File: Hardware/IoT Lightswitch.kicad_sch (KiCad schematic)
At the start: 23 parts, among them J1 Screw_Terminal_01x04, J2 Conn_01x04, K1 SANYOU_SRD_Form_C, Q1 NMOS, SW1 SW_SPDT, SW2 SW_SPDT, SW3 SW_Push, SW4 SW_Push, SW5 SW_SPST, U1 ESP32-S2-SOLO-2

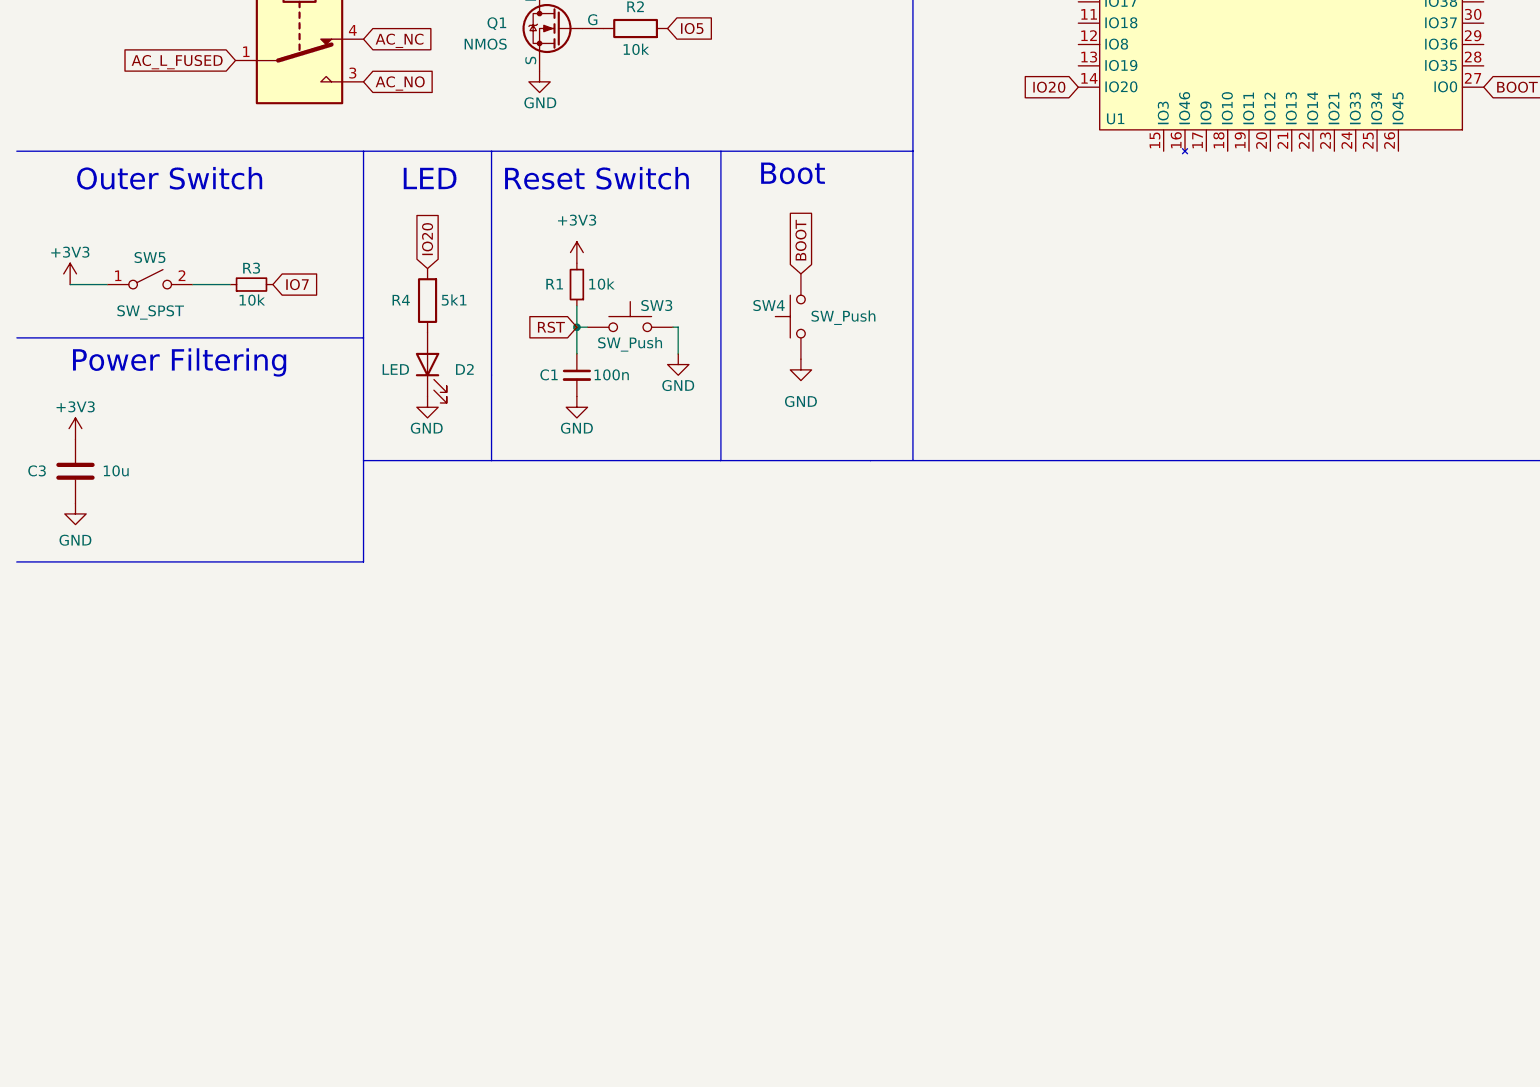
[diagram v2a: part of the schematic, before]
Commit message: Added Humidity and Temperature Sensor
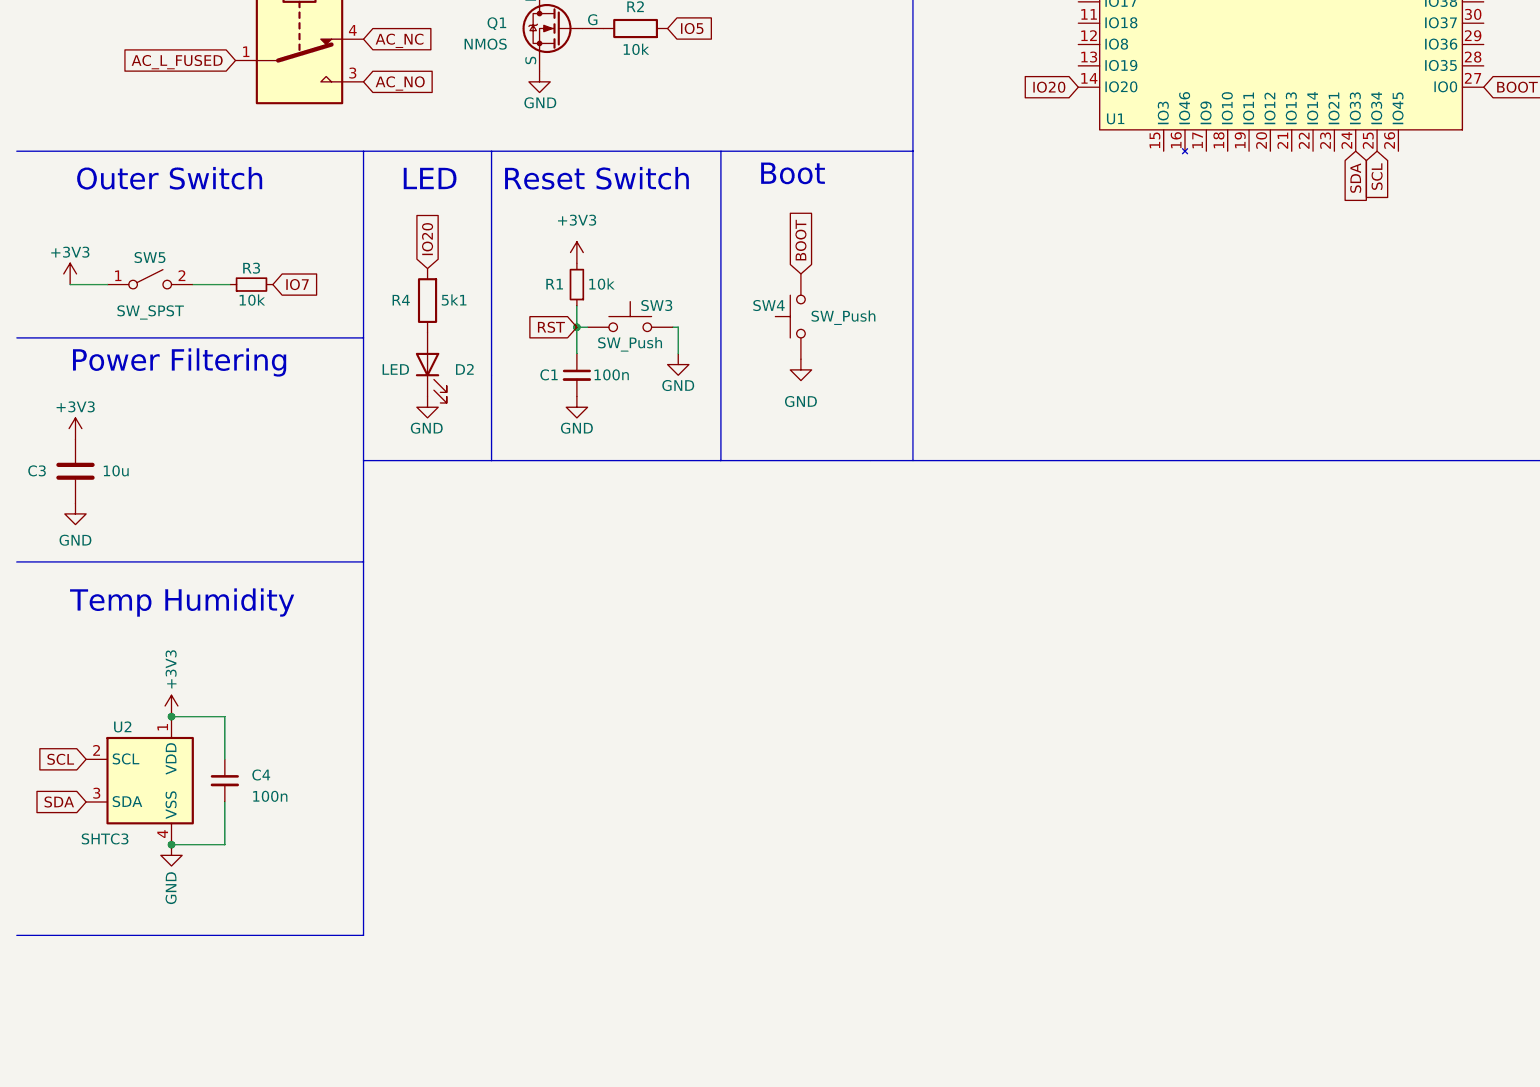
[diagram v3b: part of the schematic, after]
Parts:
- added C4: 100n, Capacitor_SMD:C_0402_1005Metric, symbol Device:C_Small
- added U2: SHTC3, Sensor_Humidity:Sensirion_DFN-4-1EP_2x2mm_P1mm_EP0.7x1.6mm, symbol Sensor_Humidity:SHTC3
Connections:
- net +3V3: now also C4.1, U2.1 (VDD)
- net GND: now also C4.2, U2.4 (VSS)
- net SDA: now reaches U1.24 (IO33)
- net SDA: now also U2.3 (SDA)
- net SCL: now reaches U1.25 (IO34)
- net SCL: now also U2.2 (SCL)
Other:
- note added: "Temp Humidity"
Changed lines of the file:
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@@
   (junction (at 86.995 30.48) (diameter 0) (color 0 0 0 0)
   )
+  (junction (at 31.115 161.29) (diameter 0) (color 0 0 0 0)
+  )
   (junction (at 187.96 36.83) (diameter 0) (color 0 0 0 0)
   )
@@
   )
   (junction (at 53.975 49.53) (diameter 0) (color 0 0 0 0)
+  )
+  (junction (at 31.115 146.05) (diameter 0) (color 0 0 0 0)
   )
   (junction (at 86.995 25.4) (diameter 0) (color 0 0 0 0)
@@
     (stroke (width 0) (type default))
   )
+  (polyline (pts (xy 12.7 172.085) (xy 53.975 172.085))
+    (stroke (width 0) (type default))
+  )
   (wire (pts (xy 91.44 102.87) (xy 91.44 99.695))
     (stroke (width 0) (type default))
   )
+  (wire (pts (xy 37.465 156.21) (xy 37.465 161.29))
+    (stroke (width 0) (type default))
+  )
   (wire (pts (xy 79.375 97.155) (xy 79.375 99.695))
     (stroke (width 0) (type default))
@@
     (stroke (width 0) (type default))
   )
+  (wire (pts (xy 37.465 161.29) (xy 31.115 161.29))
+    (stroke (width 0) (type default))
+  )
   (polyline (pts (xy 375.285 12.7) (xy 375.285 40.64))
     (stroke (width 0) (type default))
@@
   )
   (polyline (pts (xy 62.23 37.465) (xy 119.38 37.465))
+    (stroke (width 0) (type default))
+  )
+  (wire (pts (xy 31.115 146.05) (xy 37.465 146.05))
+    (stroke (width 0) (type default))
+  )
+  (polyline (pts (xy 53.975 172.085) (xy 53.975 127.635))
+    (stroke (width 0) (type default))
+  )
+  (wire (pts (xy 37.465 146.05) (xy 37.465 151.13))
     (stroke (width 0) (type default))
   )
@@
   )
   (text "LED" (at 58.42 83.82 0)
+    (effects (font (size 2.54 2.54)) (justify left bottom))
+  )
+  (text "Temp Humidity" (at 19.05 133.985 0)
     (effects (font (size 2.54 2.54)) (justify left bottom))
   )
@@
     )
   )
+  (global_label "SDA" (shape input) (at 172.085 78.74 270) (fields_autoplaced)
+    (effects (font (size 1.27 1.27)) (justify right))
+    (property "Intersheetrefs" "${INTERSHEET_REFS}" (at 172.085 85.2139 90)
+      (effects (font (size 1.27 1.27)) (justify right) hide)
+    )
+  )
   (global_label "AC_L" (shape input) (at 20.32 25.4 0) (fields_autoplaced)
     (effects (font (size 1.27 1.27)) (justify left))
@@
     )
   )
+  (global_label "SCL" (shape input) (at 20.955 151.13 180) (fields_autoplaced)
+    (effects (font (size 1.27 1.27)) (justify right))
+    (property "Intersheetrefs" "${INTERSHEET_REFS}" (at 14.5416 151.13 0)
+      (effects (font (size 1.27 1.27)) (justify right) hide)
+    )
+  )
   (global_label "AC_L_FUSED" (shape input) (at 46.355 22.86 0) (fields_autoplaced)
     (effects (font (size 1.27 1.27)) (justify left))
@@
     )
   )
+  (global_label "SCL" (shape input) (at 174.625 78.74 270) (fields_autoplaced)
+    (effects (font (size 1.27 1.27)) (justify right))
+    (property "Intersheetrefs" "${INTERSHEET_REFS}" (at 174.625 85.1534 90)
+      (effects (font (size 1.27 1.27)) (justify right) hide)
+    )
+  )
   (global_label "NEUTRAL" (shape input) (at 376.555 249.555 180) (fields_autoplaced)
     (effects (font (size 1.27 1.27)) (justify right))
@@
     )
   )
+  (global_label "SDA" (shape input) (at 20.955 156.21 180) (fields_autoplaced)
+    (effects (font (size 1.27 1.27)) (justify right))
+    (property "Intersheetrefs" "${INTERSHEET_REFS}" (at 14.4811 156.21 0)
+      (effects (font (size 1.27 1.27)) (justify right) hide)
+    )
+  )
   (global_label "IO20" (shape input) (at 139.065 71.12 180) (fields_autoplaced)
     (effects (font (size 1.27 1.27)) (justify right))
@@
         (path "/f3e717f2-cadc-4780-85c2-c75baaff6e07"
           (reference "C3") (unit 1)
+        )
+      )
+    )
+  )
+  (symbol (lib_id "Device:C_Small") (at 37.465 153.67 0) (unit 1)
+    (in_bom yes) (on_board yes) (dnp no) (fields_autoplaced)
+    (property "Reference" "C4" (at 40.64 153.0413 0)
+      (effects (font (size 1.27 1.27)) (justify left))
+    )
+    (property "Value" "100n" (at 40.64 155.5813 0)
+      (effects (font (size 1.27 1.27)) (justify left))
+    )
+    (property "Footprint" "Capacitor_SMD:C_0402_1005Metric" (at 37.465 153.67 0)
+      (effects (font (size 1.27 1.27)) hide)
+    )
+    (property "Datasheet" "~" (at 37.465 153.67 0)
+      (effects (font (size 1.27 1.27)) hide)
+    )
+    (pin "1")
+    (pin "2")
+    (instances
+      (project "IoT Lightswitch"
+        (path "/73ca29d8-df37-4de7-827e-f6dcb2458809"
+          (reference "C4") (unit 1)
         )
       )
@@
     )
   )
+  (symbol (lib_id "power:+3V3") (at 31.115 146.05 0) (unit 1)
+    (in_bom yes) (on_board yes) (dnp no)
+    (property "Reference" "#PWR019" (at 31.115 149.86 0)
+      (effects (font (size 1.27 1.27)) hide)
+    )
+    (property "Value" "+3V3" (at 31.115 142.875 90)
+      (effects (font (size 1.27 1.27)) (justify left))
+    )
+    (property "Footprint" "" (at 31.115 146.05 0)
+      (effects (font (size 1.27 1.27)) hide)
+    )
+    (property "Datasheet" "" (at 31.115 146.05 0)
+      (effects (font (size 1.27 1.27)) hide)
+    )
+    (pin "1")
+    (instances
+      (project "IoT Lightswitch"
+        (path "/73ca29d8-df37-4de7-827e-f6dcb2458809"
+          (reference "#PWR019") (unit 1)
+        )
+      )
+    )
+  )
   (symbol (lib_id "Switch:SW_SPDT") (at 396.875 237.49 180) (unit 1)
     (in_bom no) (on_board no) (dnp no) (fields_autoplaced)
@@
     )
   )
+  (symbol (lib_id "Sensor_Humidity:SHTC3") (at 28.575 153.67 0) (unit 1)
+    (in_bom yes) (on_board yes) (dnp no)
+    (property "Reference" "U2" (at 24.13 147.32 0)
+      (effects (font (size 1.27 1.27)) (justify left))
+    )
+    (property "Value" "SHTC3" (at 20.32 160.655 0)
+      (effects (font (size 1.27 1.27)) (justify left))
+    )
+    (property "Footprint" "Sensor_Humidity:Sensirion_DFN-4-1EP_2x2mm_P1mm_EP0.7x1.6mm" (at 33.655 162.56 0)
+      (effects (font (size 1.27 1.27)) hide)
+    )
+    (property "Datasheet" "https://www.sensirion.com/fileadmin/user_upload/customers/sensirion/Dokumente/0_Datasheets/Humidity/Sensirion_Humidity_Sensors_SHTC3_Datasheet.pdf" (at 20.955 142.24 0)
+      (effects (font (size 1.27 1.27)) hide)
+    )
+    (pin "1")
+    (pin "2")
+    (pin "3")
+    (pin "4")
+    (pin "5")
+    (instances
+      (project "IoT Lightswitch"
+        (path "/73ca29d8-df37-4de7-827e-f6dcb2458809"
+          (reference "U2") (unit 1)
+        )
+      )
+    )
+  )
   (symbol (lib_id "power:GND") (at 91.44 102.87 0) (unit 1)
     (in_bom yes) (on_board yes) (dnp no)
@@
         )
       )
+    )
+  )
+  (symbol (lib_id "power:GND") (at 31.115 161.29 0) (unit 1)
+    (in_bom yes) (on_board yes) (dnp no)
+    (property "Reference" "#PWR018" (at 31.115 167.64 0)
+      (effects (font (size 1.27 1.27)) hide)
+    )
+    (property "Value" "GND" (at 31.115 164.465 90)
+      (effects (font (size 1.27 1.27)) (justify right))
+    )
+    (property "Footprint" "" (at 31.115 161.29 0)
+      (effects (font (size 1.27 1.27)) hide)
+    )
+    (property "Datasheet" "" (at 31.115 161.29 0)
+      (effects (font (size 1.27 1.27)) hide)
+    )
+    (pin "1")
+    (instances
+      (project "IoT Lightswitch"
+        (path "/73ca29d8-df37-4de7-827e-f6dcb2458809"
+          (reference "#PWR018") (unit 1)
+        )
+      )
